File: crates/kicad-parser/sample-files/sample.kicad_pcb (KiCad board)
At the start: 2 copper layers, 41 x 33 mm, 0 parts

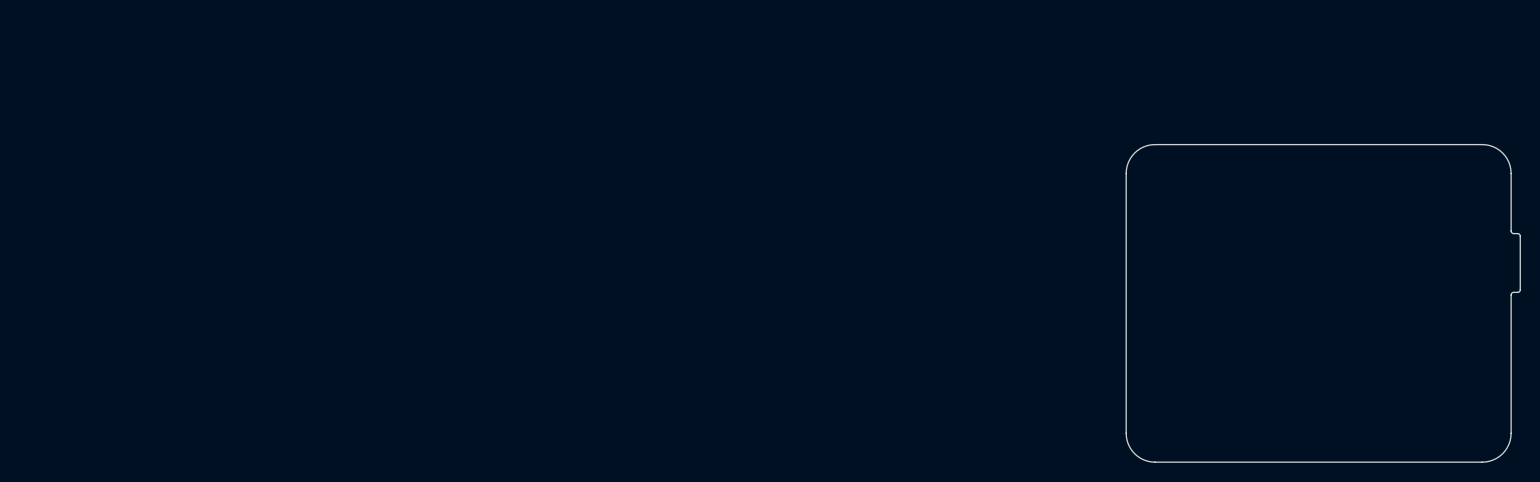
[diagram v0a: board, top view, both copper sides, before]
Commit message: more graphics; to primatives for graphics
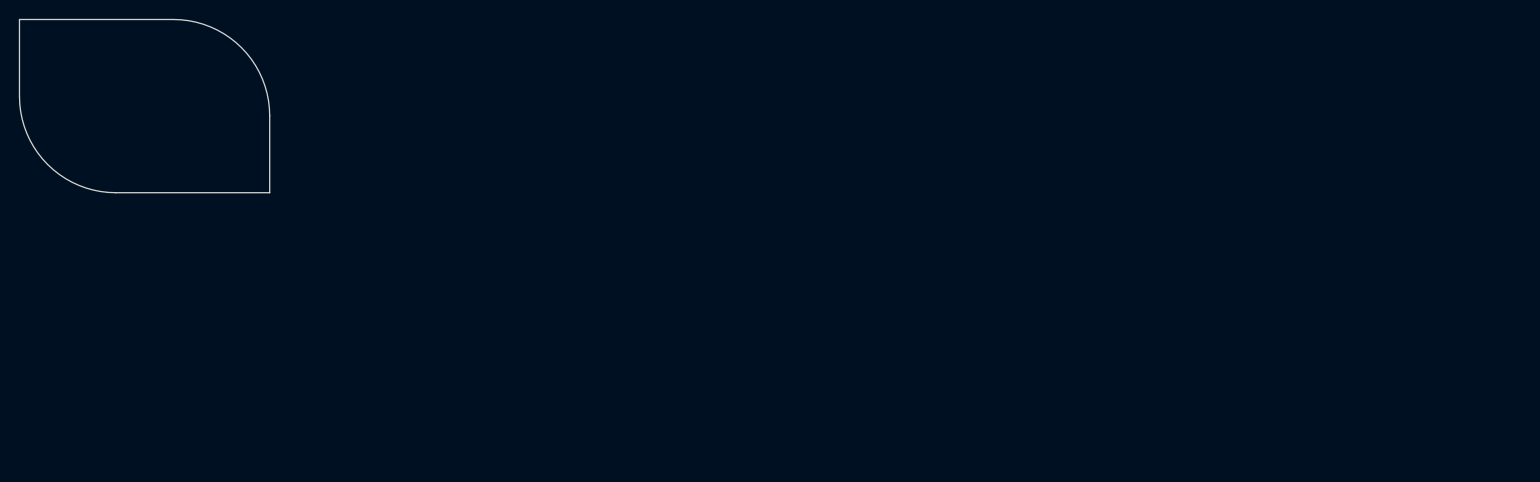
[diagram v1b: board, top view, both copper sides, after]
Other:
- board size 41 x 33 mm -> 26 x 18 mm
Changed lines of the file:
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@@
-(kicad_pcb
-  (version 20221018)
-  (generator pcbnew)
+(kicad_pcb (version 20221018) (generator pcbnew)
   (general
     (thickness 0.89)
@@
     (58 "User.9" user)
   )
-  (gr_line (start 174.8 55.1) (end 174.35 55.55)
-    (stroke (width 0.1) (type default)) (layer "B.SilkS"))
-  (gr_line (start 157 56.35) (end 157 56.1)
-    (stroke (width 0.1) (type default)) (layer "B.SilkS"))
-  (gr_line (start 174.35 55.55) (end 174.35 55.2)
-    (stroke (width 0.1) (type default)) (layer "B.SilkS"))
-  (gr_line (start 156.55 55.9) (end 157 56.35)
-    (stroke (width 0.1) (type default)) (layer "B.SilkS"))
-  (gr_line (start 185 71) (end 151 71)
-    (stroke (width 0.1) (type default)) (layer "Edge.Cuts"))
-  (gr_line (start 188.950546 53.08) (end 188.950546 47.524454)
-    (stroke (width 0.1) (type default)) (layer "Edge.Cuts"))
-  (gr_arc (start 188.675546 47.249454) (mid 188.87 47.33) (end 188.950546 47.524454)
-    (stroke (width 0.1) (type default)) (layer "Edge.Cuts"))
-  (gr_arc (start 188 68) (mid 187.12132 70.12132) (end 185 71)
-    (stroke (width 0.1) (type default)) (layer "Edge.Cuts"))
-  (gr_arc (start 148 41) (mid 148.87868 38.87868) (end 151 38)
-    (stroke (width 0.1) (type default)) (layer "Edge.Cuts"))
-  (gr_line (start 188 46.973866) (end 188 41)
-    (stroke (width 0.1) (type default)) (layer "Edge.Cuts"))
-  (gr_arc (start 188.950546 53.08) (mid 188.87 53.274454) (end 188.675546 53.355)
-    (stroke (width 0.1) (type default)) (layer "Edge.Cuts"))
-  (gr_line (start 151 38) (end 185 38)
-    (stroke (width 0.1) (type default)) (layer "Edge.Cuts"))
-  (gr_line (start 188 53.64) (end 188 68)
-    (stroke (width 0.1) (type default)) (layer "Edge.Cuts"))
-  (gr_arc (start 151 71) (mid 148.87868 70.12132) (end 148 68)
-    (stroke (width 0.1) (type default)) (layer "Edge.Cuts"))
-  (gr_line (start 148 68) (end 148 41)
-    (stroke (width 0.1) (type default)) (layer "Edge.Cuts"))
-  (gr_arc (start 185 38) (mid 187.12132 38.87868) (end 188 41)
-    (stroke (width 0.1) (type default)) (layer "Edge.Cuts"))
-  (gr_line (start 188.675546 53.355588) (end 188.275 53.355588)
-    (stroke (width 0.1) (type default)) (layer "Edge.Cuts"))
-  (gr_arc (start 188 53.630588) (mid 188.080546 53.436134) (end 188.275 53.355588)
-    (stroke (width 0.1) (type default)) (layer "Edge.Cuts"))
-  (gr_line (start 188.275 47.248866) (end 188.675546 47.248866)
-    (stroke (width 0.1) (type default)) (layer "Edge.Cuts"))
-  (gr_arc (start 188.275 47.248866) (mid 188.080546 47.16832) (end 188 46.973866)
-    (stroke (width 0.1) (type default)) (layer "Edge.Cuts"))
+  (setup
+    (pad_to_mask_clearance 0)
+    (pcbplotparams
+      (layerselection 0x00010fc_ffffffff)
+      (plot_on_all_layers_selection 0x0000000_00000000)
+      (disableapertmacros false)
+      (usegerberextensions false)
+      (usegerberattributes true)
+      (usegerberadvancedattributes true)
+      (creategerberjobfile true)
+      (dashed_line_dash_ratio 12.000000)
+      (dashed_line_gap_ratio 3.000000)
+      (svgprecision 4)
+      (plotframeref false)
+      (viasonmask false)
+      (mode 1)
+      (useauxorigin false)
+      (hpglpennumber 1)
+      (hpglpenspeed 20)
+      (hpglpendiameter 15.000000)
+      (dxfpolygonmode true)
+      (dxfimperialunits true)
+      (dxfusepcbnewfont true)
+      (psnegative false)
+      (psa4output false)
+      (plotreference true)
+      (plotvalue true)
+      (plotinvisibletext false)
+      (sketchpadsonfab false)
+      (subtractmaskfromsilk false)
+      (outputformat 1)
+      (mirror false)
+      (drillshape 1)
+      (scaleselection 1)
+      (outputdirectory "")
+    )
+  )
+  (net 0 "")
+  (gr_line (start 59 35) (end 59 43)
+    (stroke (width 0.05) (type default)) (layer "Edge.Cuts"))
+  (gr_line (start 59 43) (end 43 43)
+    (stroke (width 0.05) (type default)) (layer "Edge.Cuts"))
+  (gr_line (start 33 33) (end 33 25)
+    (stroke (width 0.05) (type default)) (layer "Edge.Cuts"))
+  (gr_arc (start 49 25) (mid 56.071068 27.928932) (end 59 35)
+    (stroke (width 0.05) (type default)) (layer "Edge.Cuts"))
+  (gr_arc (start 43 43) (mid 35.928932 40.071068) (end 33 33)
+    (stroke (width 0.05) (type default)) (layer "Edge.Cuts"))
+  (gr_line (start 33 25) (end 49 25)
+    (stroke (width 0.05) (type default)) (layer "Edge.Cuts"))
 )
